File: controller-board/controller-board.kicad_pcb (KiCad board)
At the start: 2 copper layers, 130 x 95 mm, 96 parts, among them J1 Conn_01x02, J2 Conn_01x02, J3 Conn_01x02, J4 Conn_01x02, J5 Conn_01x03, J6 Conn_01x02, J7 Conn_01x02, Q1 PMV45EN2, Q3 RQ3E120ATTB, U1 CAT4201, U2 PocketBeagle, U3 LTC3624, U4 CAT4201, U5 CAT4201, U6 CAT4201, U7 MCP4728, U8 ADC108S022

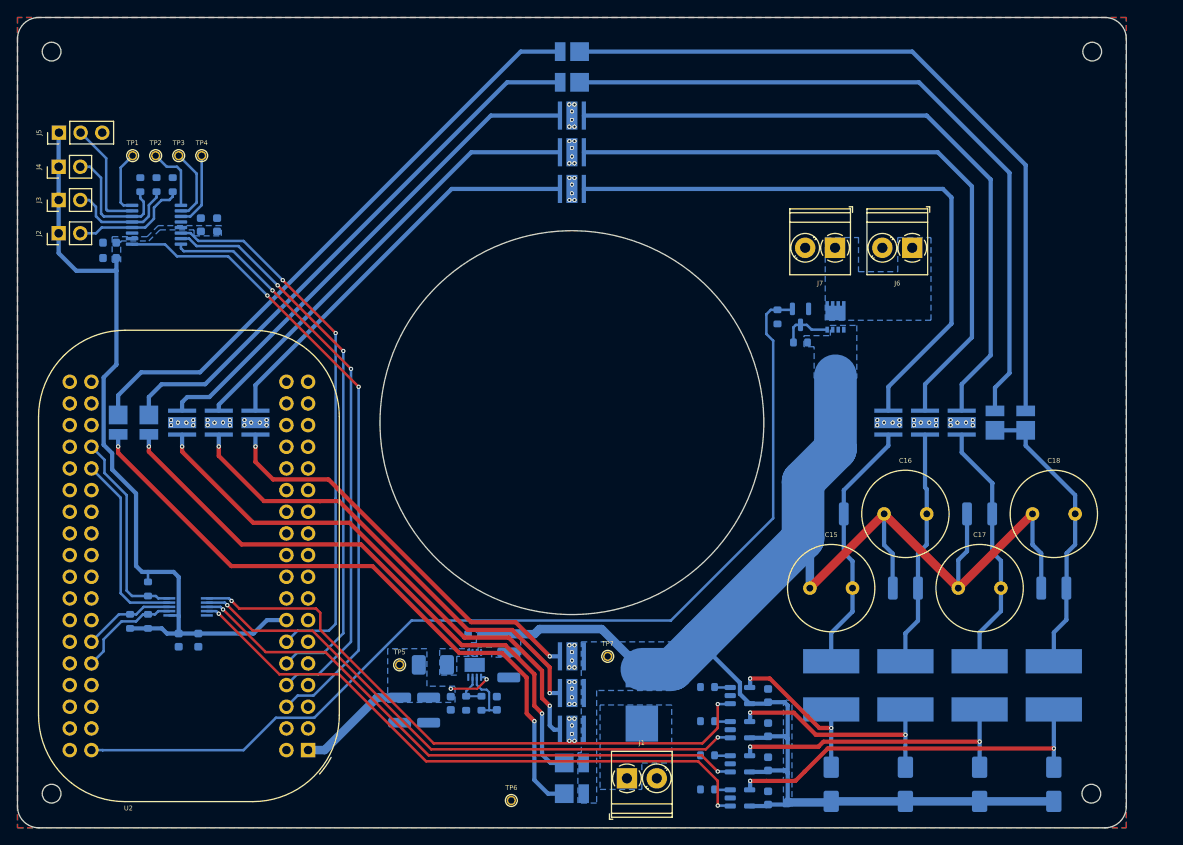
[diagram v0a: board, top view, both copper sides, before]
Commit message: Updated controller board and added BOM
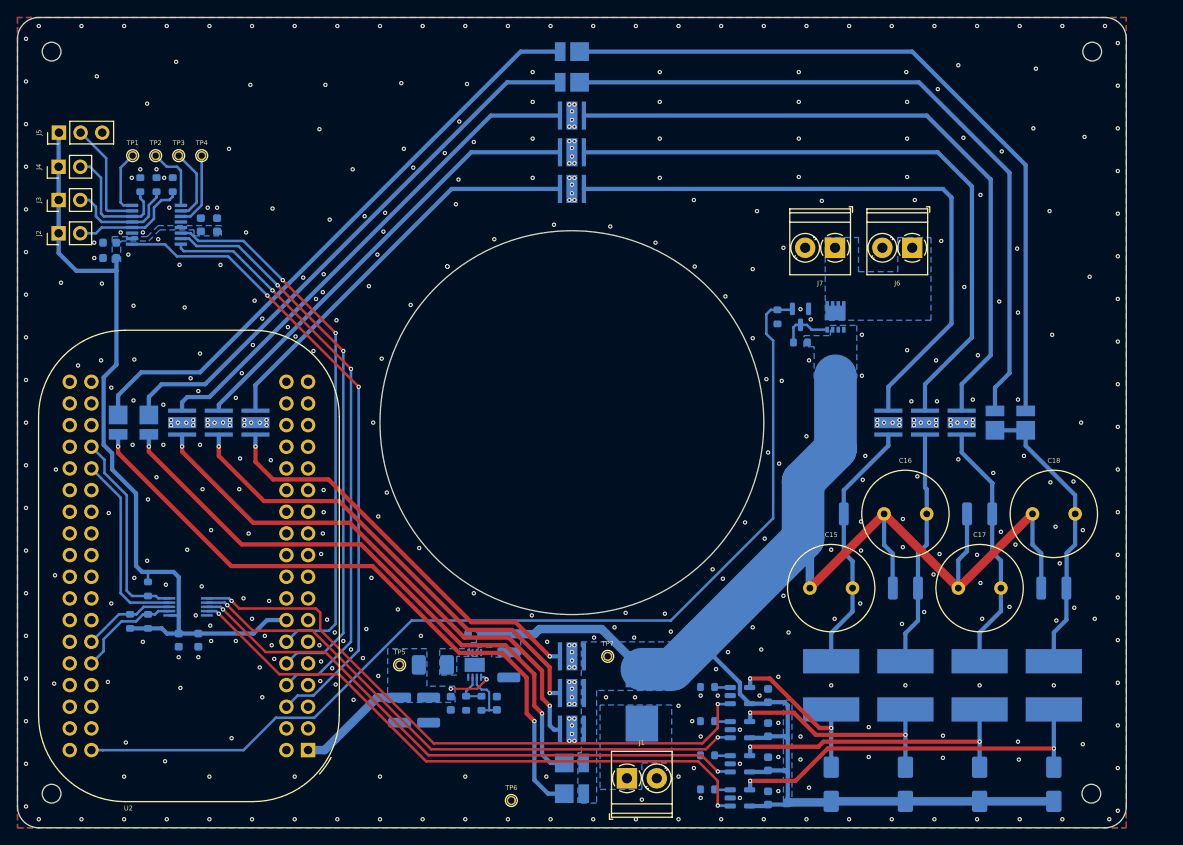
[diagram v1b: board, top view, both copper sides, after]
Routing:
- net GND: vias 72 -> 449
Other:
- board text removed: "Todo: Add stitching vias, and figure out heat sinks Pull back GND plane around mounting holes"

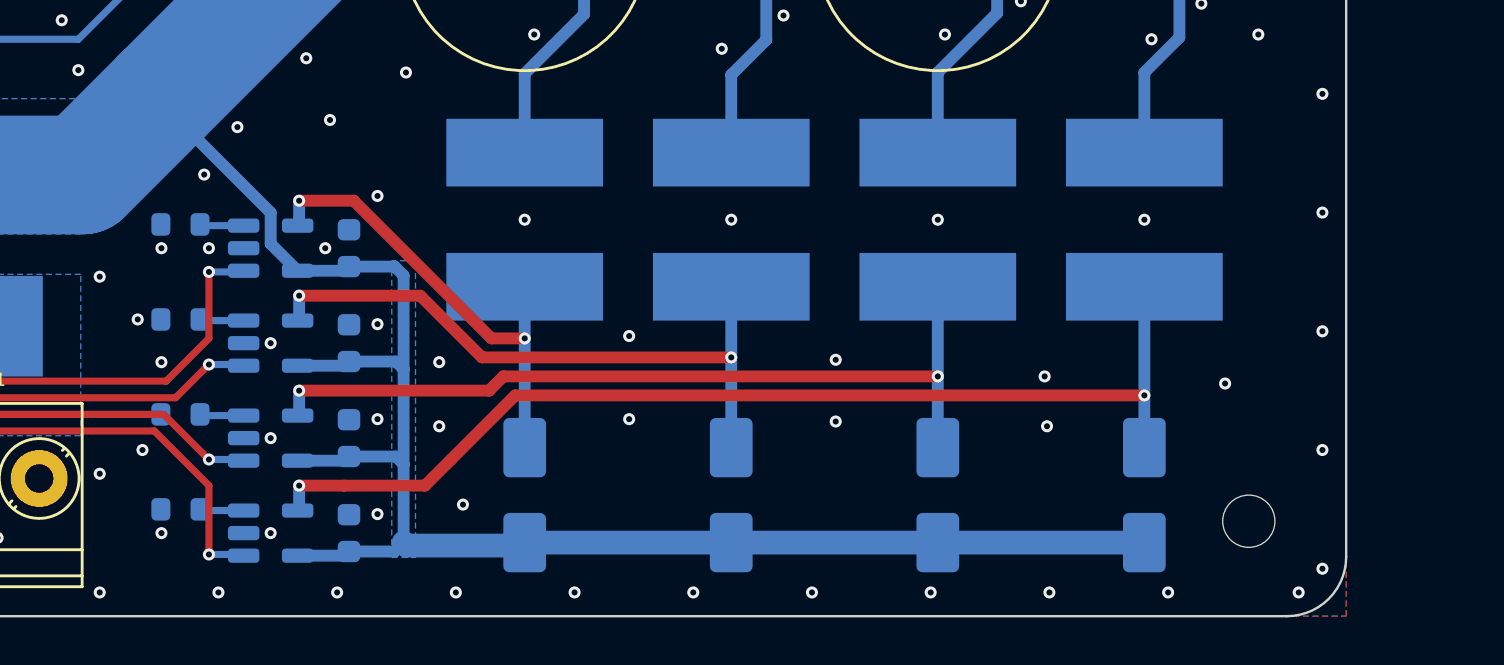
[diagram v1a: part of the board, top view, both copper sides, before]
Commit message: Added silk screen name/date
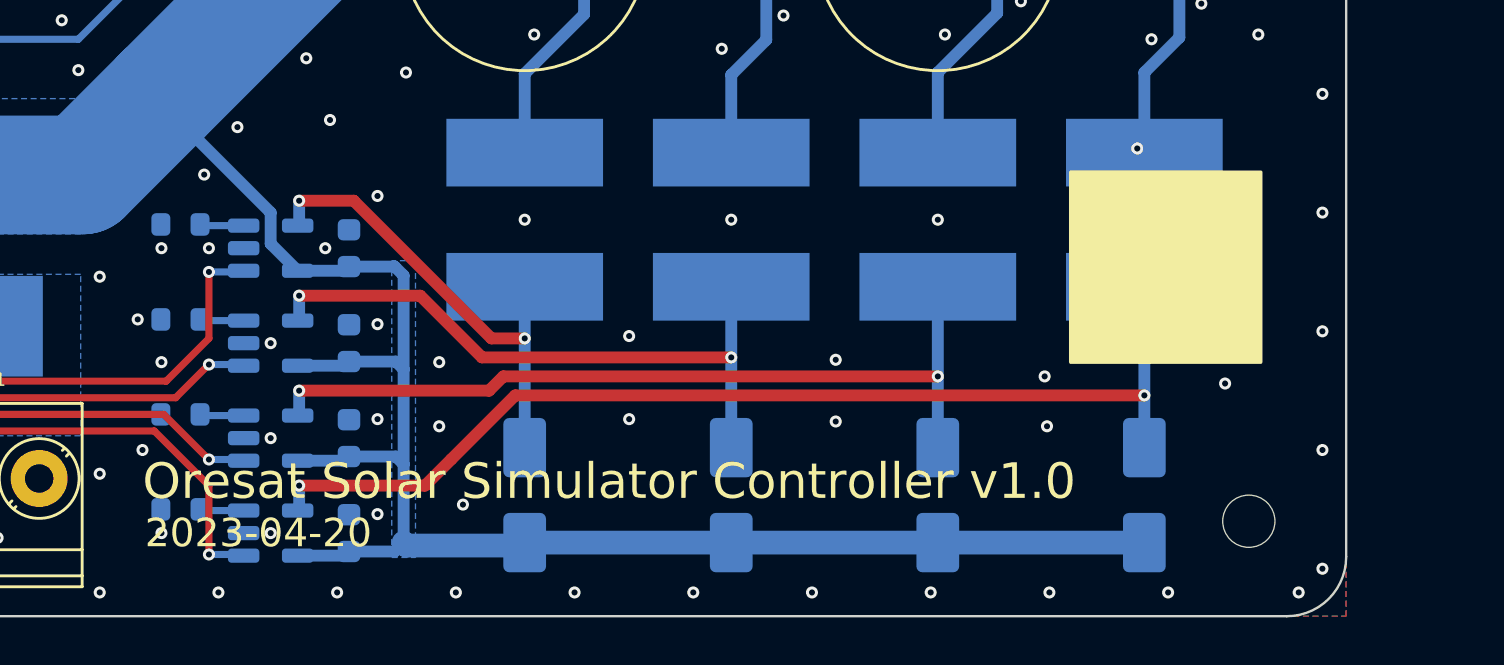
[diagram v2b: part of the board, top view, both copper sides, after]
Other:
- board text added: "2023-04-20"
- board text added: "Oresat Solar Simulator Controller v1.0"
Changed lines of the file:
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@@
     )
   )
+  (gr_rect (start 198.4 131.3) (end 206.4 139.3)
+    (stroke (width 0.15) (type solid)) (fill solid) (layer "F.SilkS"))
   (gr_line (start 210 57.5) (end 210 147.5)
     (stroke (width 0.1) (type default)) (layer "Edge.Cuts"))
@@
   (gr_arc (start 82.5 150) (mid 80.732233 149.267767) (end 80 147.5)
     (stroke (width 0.1) (type default)) (layer "Edge.Cuts"))
+  (gr_text "Oresat Solar Simulator Controller v1.0" (at 159.3 145.2) (layer "F.SilkS")
+    (effects (font (size 1.5 1.5) (thickness 0.2)) (justify left bottom))
+  )
+  (gr_text "2023-04-20" (at 159.4 147.2) (layer "F.SilkS")
+    (effects (font (size 1.2 1.2) (thickness 0.18)) (justify left bottom))
+  )
   (segment (start 199 113.2) (end 190.3 121.9) (width 1) (layer "F.Cu") (net 1))
   (segment (start 181.6 113.2) (end 190.3 121.9) (width 1) (layer "F.Cu") (net 1))
@@
   (via (at 102.3 102.2) (size 0.508) (drill 0.254) (layers "F.Cu" "B.Cu") (net 2))
   (via (at 87.5 149) (size 0.508) (drill 0.254) (layers "F.Cu" "B.Cu") (free) (net 2))
-  (via (at 201.5 133.3) (size 0.508) (drill 0.254) (layers "F.Cu" "B.Cu") (free) (net 2))
+  (via (at 201.2 130.3) (size 0.508) (drill 0.254) (layers "F.Cu" "B.Cu") (free) (net 2))
   (via (at 81 147.5) (size 0.508) (drill 0.254) (layers "F.Cu" "B.Cu") (free) (net 2))
   (via (at 162.1 134.5) (size 0.508) (drill 0.254) (layers "F.Cu" "B.Cu") (free) (net 2))
@@
         (xy 208.025037 146.569402)
         (xy 208.081179 146.287158)
-        (xy 208.1 146)
       )
     )
@@
         (xy 86.125037 146.569402)
         (xy 86.181179 146.287158)
-        (xy 86.2 146)
       )
     )
@@
         (xy 208.125037 59.569402)
         (xy 208.181179 59.287158)
-        (xy 208.2 59)
       )
     )
@@
         (xy 86.12643 59.548144)
         (xy 86.182572 59.2659)
-        (xy 86.201393 58.978742)
       )
     )
